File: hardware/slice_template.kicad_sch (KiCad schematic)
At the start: 19 parts, among them J1 Conn_01x10_Socket, SW1 SW_DIP_x04, U1 AP63205

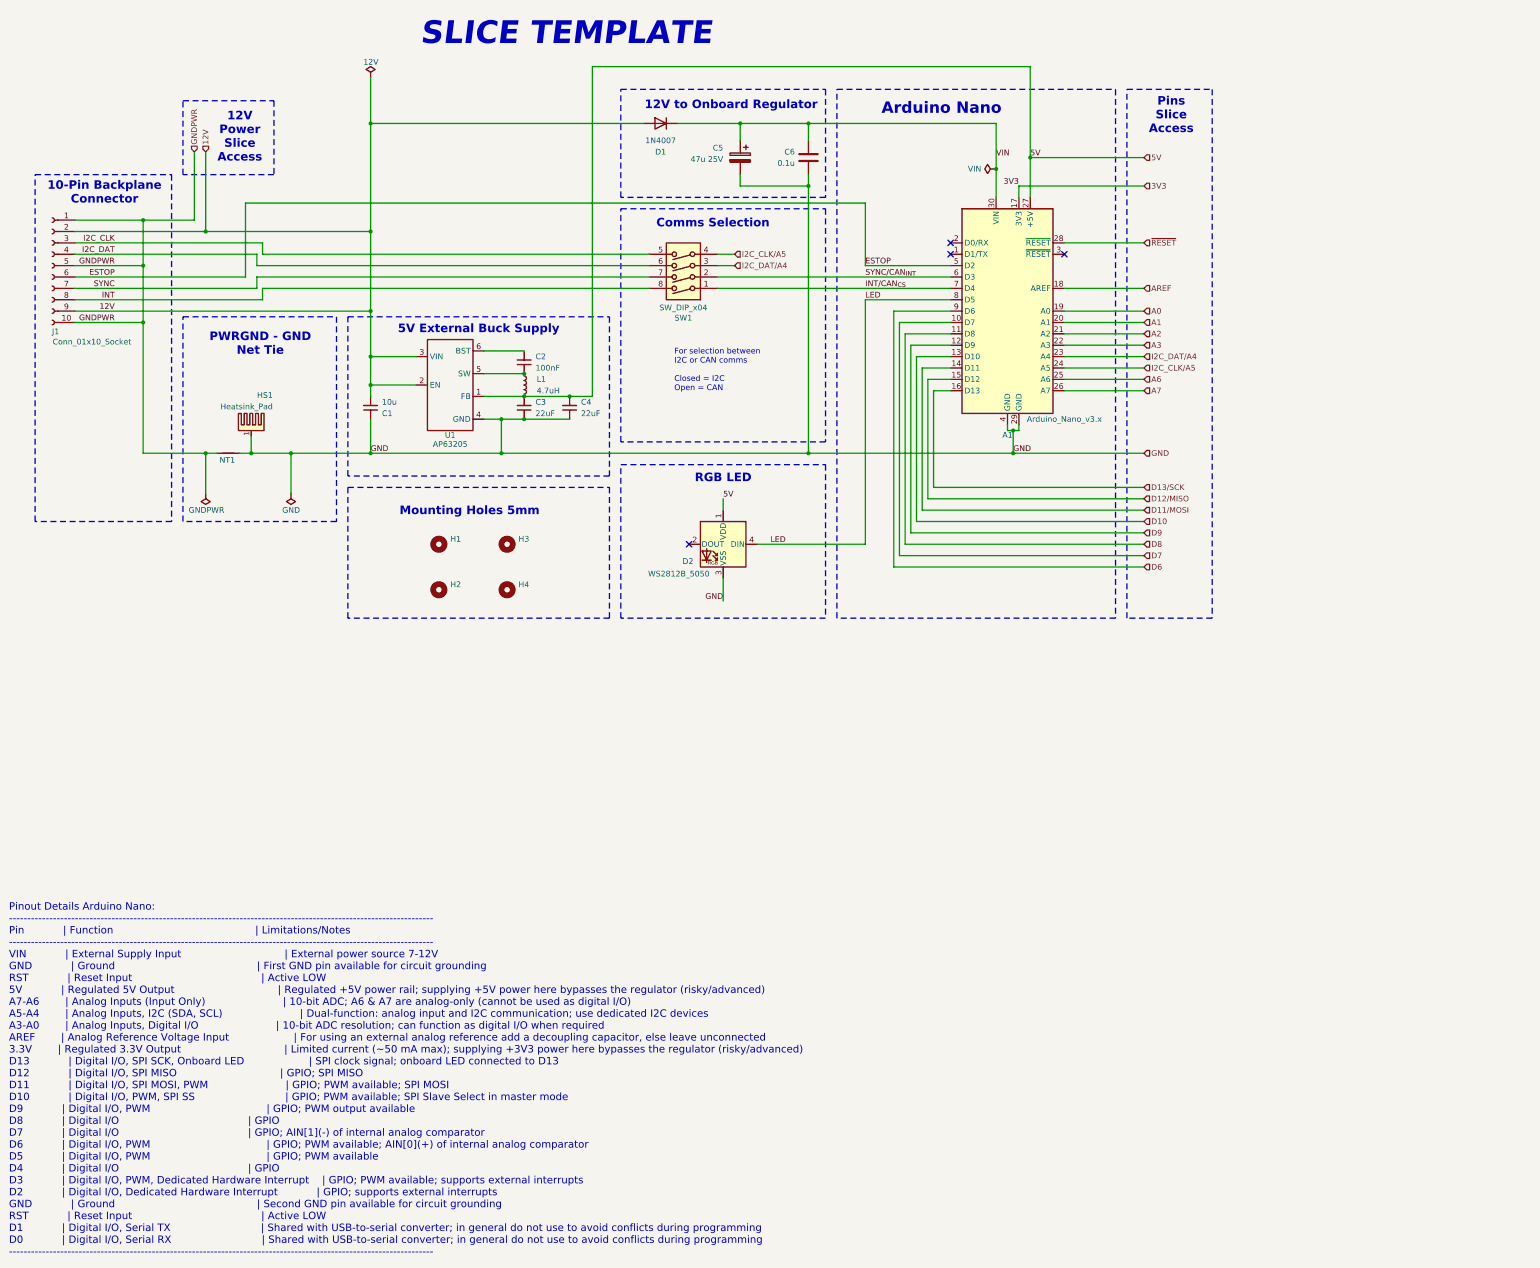
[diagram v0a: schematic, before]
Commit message: Changed to Pico from nano
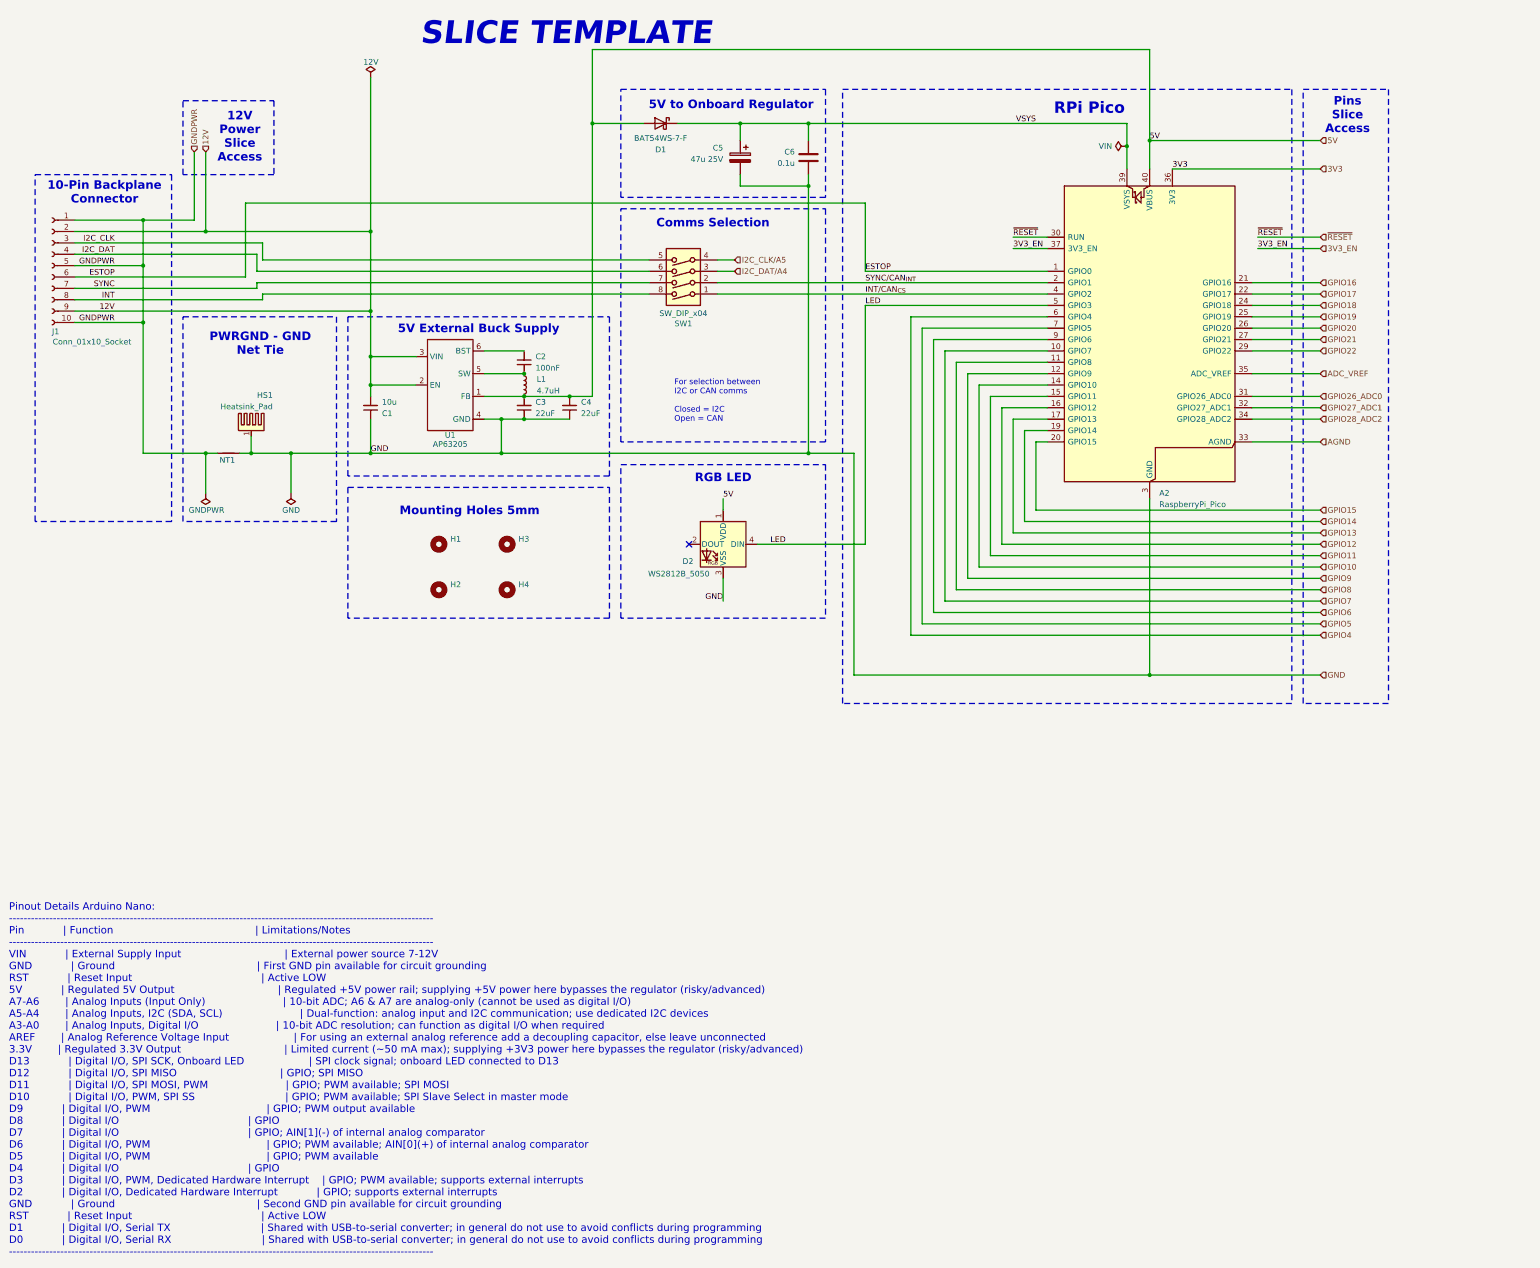
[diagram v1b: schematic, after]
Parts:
- removed A1: Arduino_Nano_v3.x, KMLib_Boards_Modules:Arduino_Nano_Headers, symbol kml-custom:Arduino_Nano_v3.x
- removed D1: 1N4007, Diode_SMD:D_SOD-123F, symbol Diode:1N4007
- added A2: RaspberryPi_Pico, Module:RaspberryPi_Pico_Common_Unspecified, symbol MCU_Module:RaspberryPi_Pico
- added D1: BAT54WS-7-F, Diode_SMD:D_SOD-323_HandSoldering, symbol Device:D_Schottky
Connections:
- net 3V3: now also A2.36 (3V3)
- net 5V: now also A2.40 (VBUS), D1.2 (A)
- net ESTOP: now also A2.1 (GPIO0)
- net GND: now also A2.13 (GND), A2.18 (GND), A2.23 (GND), A2.28 (GND), A2.3 (GND), A2.38 (GND), A2.8 (GND)
- net INT/CAN_{CS}: now also A2.4 (GPIO2)
- net LED: now also A2.5 (GPIO3)
- net SYNC/CAN_{INT}: now also A2.2 (GPIO1)
- net ~{RESET}: now also A2.30 (RUN)
- net VIN renamed VSYS
- net VSYS: now also A2.39 (VSYS), D1.1 (K)
- new net 3V3_EN: A2.37 (3V3_EN)
- new net ADC_VREF: A2.35 (ADC_VREF)
- new net AGND: A2.33 (AGND)
- new net GPIO10: A2.14 (GPIO10)
- new net GPIO11: A2.15 (GPIO11)
- new net GPIO12: A2.16 (GPIO12)
- new net GPIO13: A2.17 (GPIO13)
- new net GPIO14: A2.19 (GPIO14)
- new net GPIO15: A2.20 (GPIO15)
- new net GPIO16: A2.21 (GPIO16)
- new net GPIO17: A2.22 (GPIO17)
- new net GPIO18: A2.24 (GPIO18)
- new net GPIO19: A2.25 (GPIO19)
- new net GPIO20: A2.26 (GPIO20)
- new net GPIO21: A2.27 (GPIO21)
- new net GPIO22: A2.29 (GPIO22)
- new net GPIO26_ADC0: A2.31 (GPIO26_ADC0)
- new net GPIO27_ADC1: A2.32 (GPIO27_ADC1)
- new net GPIO28_ADC2: A2.34 (GPIO28_ADC2)
- new net GPIO4: A2.6 (GPIO4)
- new net GPIO5: A2.7 (GPIO5)
- new net GPIO6: A2.9 (GPIO6)
- new net GPIO7: A2.10 (GPIO7)
- new net GPIO8: A2.11 (GPIO8)
- new net GPIO9: A2.12 (GPIO9)
- no-connect marks 4 -> 1
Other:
- note added: "5V to Onboard Regulator"
- note added: "RPi Pico"
- note removed: "12V to Onboard Regulator"
- note removed: "Arduino Nano"
- moved on the sheet: SW1

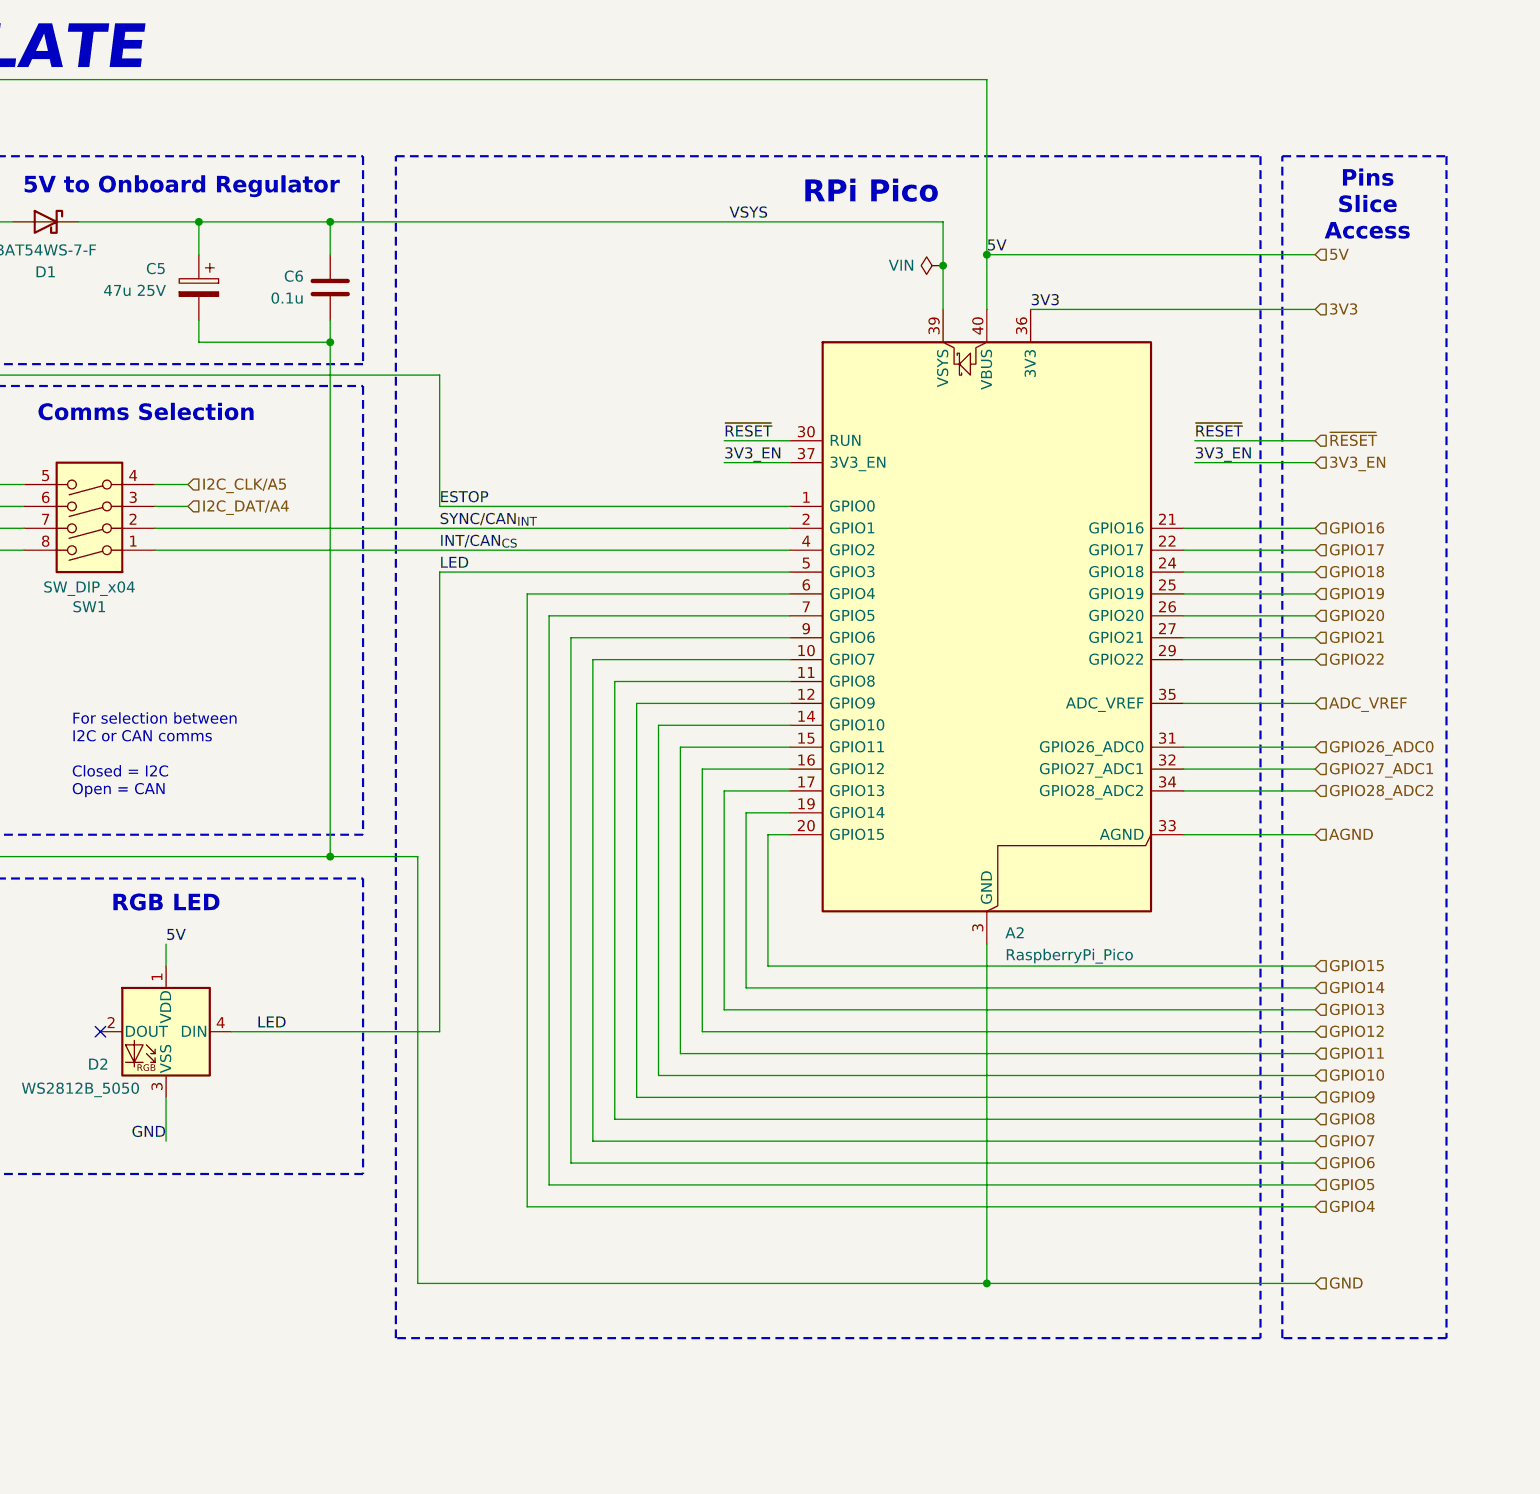
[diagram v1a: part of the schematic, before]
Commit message: added i2c and spi
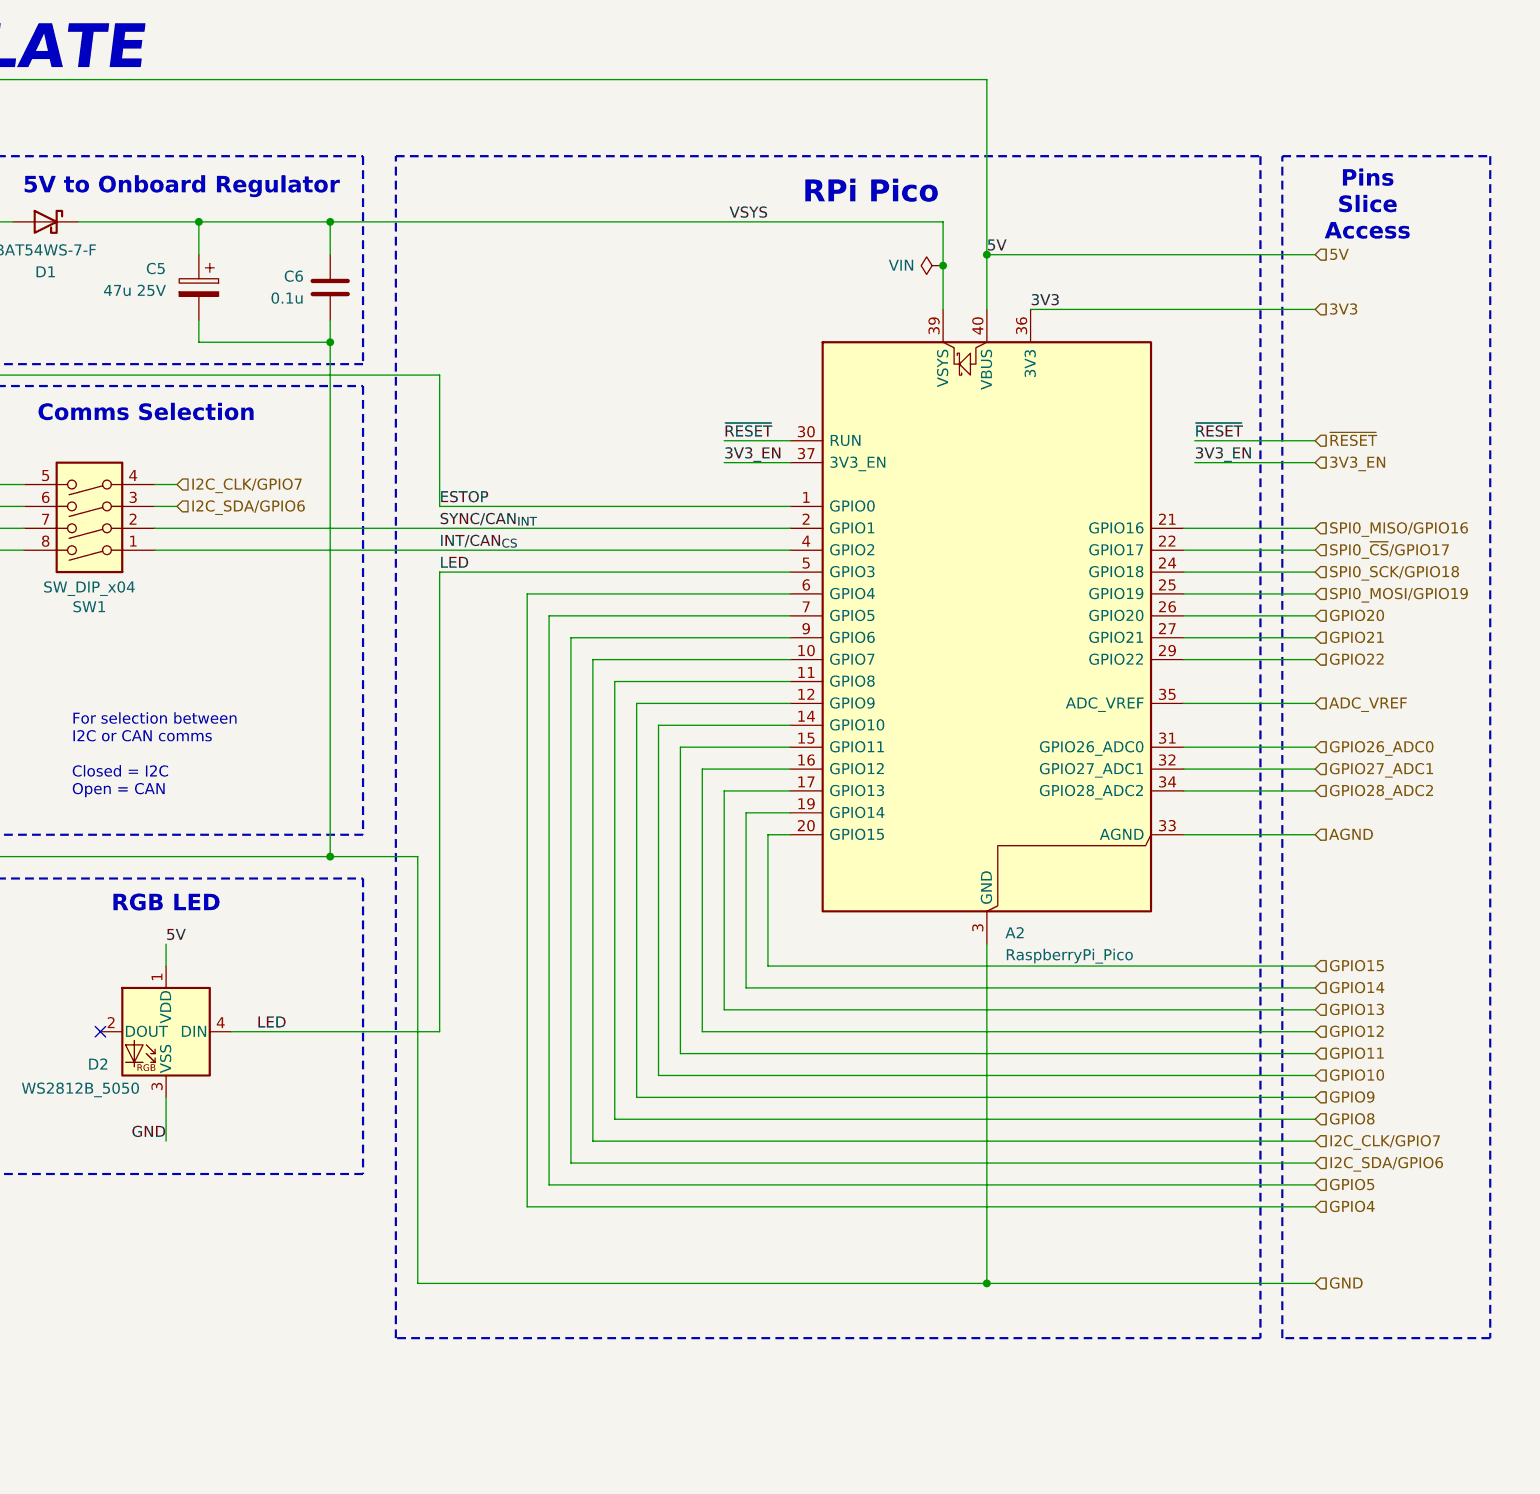
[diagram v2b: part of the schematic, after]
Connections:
- net I2C_CLK/A5 is gone; now on net I2C_CLK/GPIO7: SW1.4
- net I2C_DAT/A4 is gone; now on net I2C_SDA/GPIO6: SW1.3
- net GPIO16 renamed SPI0_MISO/GPIO16
- net GPIO17 renamed SPI0_~{CS}/GPIO17
- net GPIO18 renamed SPI0_SCK/GPIO18
- net GPIO19 renamed SPI0_MOSI/GPIO19
- net GPIO6 renamed I2C_SDA/GPIO6
- net GPIO7 renamed I2C_CLK/GPIO7
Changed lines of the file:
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@@
 	(rectangle
 		(start 303.53 31.75)
-		(end 322.58 168.91)
+		(end 327.66 168.91)
 		(stroke
 			(width 0.254)
@@
 	(wire
 		(pts
-			(xy 172.72 72.39) (xy 176.53 72.39)
+			(xy 172.72 72.39) (xy 175.26 72.39)
 		)
 		(stroke
@@
 	(wire
 		(pts
-			(xy 172.72 69.85) (xy 176.53 69.85)
+			(xy 172.72 69.85) (xy 175.26 69.85)
 		)
 		(stroke
@@
 		)
 	)
-	(hierarchical_label "GPIO18"
+	(hierarchical_label "SPI0_SCK{slash}GPIO18"
 		(shape input)
 		(at 307.34 80.01 0)
@@
 		)
 	)
-	(hierarchical_label "GPIO7"
+	(hierarchical_label "I2C_CLK{slash}GPIO7"
 		(shape input)
 		(at 307.34 146.05 0)
@@
 		)
 	)
-	(hierarchical_label "GPIO6"
+	(hierarchical_label "I2C_SDA{slash}GPIO6"
 		(shape input)
 		(at 307.34 148.59 0)
@@
 		)
 	)
-	(hierarchical_label "GPIO16"
+	(hierarchical_label "SPI0_MISO{slash}GPIO16"
 		(shape input)
 		(at 307.34 74.93 0)
@@
 		)
 	)
-	(hierarchical_label "I2C_DAT{slash}A4"
-		(shape input)
-		(at 176.53 72.39 0)
+	(hierarchical_label "I2C_SDA{slash}GPIO6"
+		(shape input)
+		(at 175.26 72.39 0)
 		(effects
 			(font
@@
 		)
 	)
-	(hierarchical_label "GPIO17"
+	(hierarchical_label "SPI0_~{CS}{slash}GPIO17"
 		(shape input)
 		(at 307.34 77.47 0)
@@
 		)
 	)
-	(hierarchical_label "I2C_CLK{slash}A5"
-		(shape input)
-		(at 176.53 69.85 0)
-		(effects
-			(font
-				(size 1.27 1.27)
-			)
-			(justify left)
-		)
-	)
-	(hierarchical_label "GPIO19"
+	(hierarchical_label "I2C_CLK{slash}GPIO7"
+		(shape input)
+		(at 175.26 69.85 0)
+		(effects
+			(font
+				(size 1.27 1.27)
+			)
+			(justify left)
+		)
+	)
+	(hierarchical_label "SPI0_MOSI{slash}GPIO19"
 		(shape input)
 		(at 307.34 82.55 0)

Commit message: added level shifter and started layout
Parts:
- added C7: 100nF, Capacitor_SMD:C_1206_3216Metric, symbol Device:C_Small
- added R1, R2: 4.7k, Resistor_SMD:R_0603_1608Metric_Pad0.98x0.95mm_HandSolder, symbol Device:R
- added R3: 200k, Resistor_SMD:R_0603_1608Metric_Pad0.98x0.95mm_HandSolder, symbol Device:R
- added U2: PCA9306DC1, Package_SO:VSSOP-8_2.3x2mm_P0.5mm, symbol Interface:PCA9306DC1
- A2: footprint Module:RaspberryPi_Pico_Common_Unspecified -> KMLib_Boards_Modules:RaspberryPi_Pico_THT
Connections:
- net 3V3: now also R1.1, R2.1, U2.2 (VREF1)
- net 5V: now also R3.1
- net GND: now also C7.1, U2.1 (GND)
- net I2C_CLK: now also U2.6 (SCL2); no longer SW1.5
- net I2C_DAT: now also U2.5 (SDA2); no longer SW1.6
- net GPIO20 renamed I2C0_SDA/GPIO20
- net I2C0_SDA/GPIO20: now also SW1.3
- net GPIO21 renamed I2C0_CLK/GPIO21
- net I2C0_CLK/GPIO21: now also SW1.4
- net I2C_CLK/GPIO7 renamed GPIO7
- net GPIO7: no longer SW1.4
- net I2C_SDA/GPIO6 renamed GPIO6
- net GPIO6: no longer SW1.3
- new net: R1.2, SW1.5, U2.3 (SCL1)
- new net: R2.2, SW1.6, U2.4 (SDA1)
- new net: C7.2, R3.2, U2.7 (VREF2), U2.8 (EN)
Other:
- note added: "I2C Level Shifter"
- moved on the sheet: A2, C1, C2, C3, C4, C5, C6, D1, D2, H1, H2, H3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
